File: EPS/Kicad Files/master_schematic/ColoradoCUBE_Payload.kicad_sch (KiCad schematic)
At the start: 8 parts, among them U1 PIC18F27Q84-E/SP

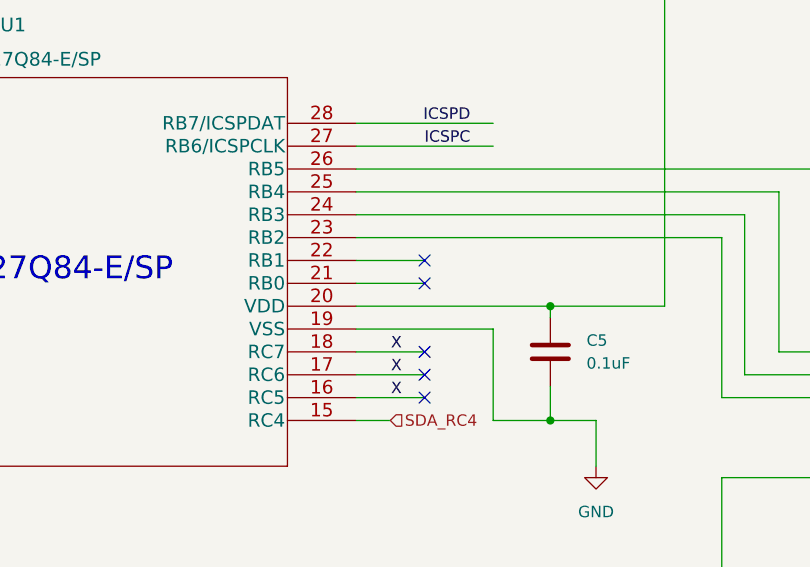
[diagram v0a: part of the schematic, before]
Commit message: revised EPS schematics
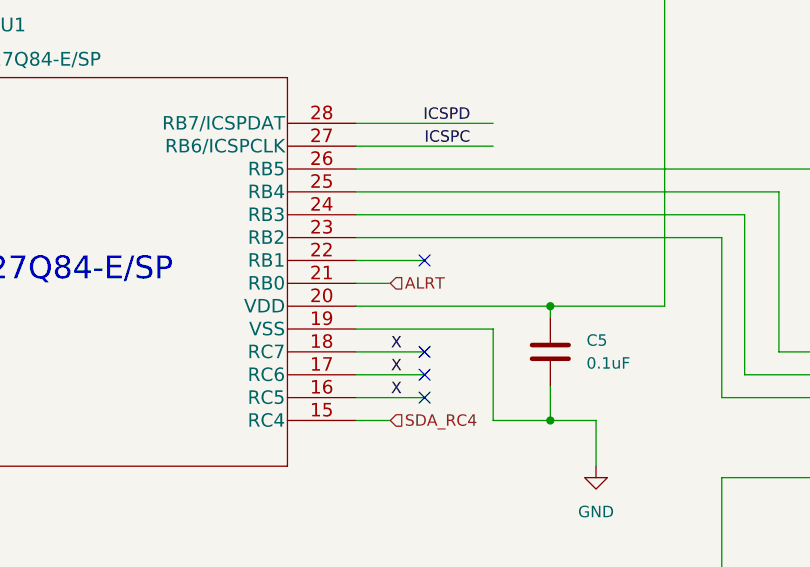
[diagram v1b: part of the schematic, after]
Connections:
- net ALRT: now reaches U1.21 (RB0)
- no-connect marks 11 -> 10
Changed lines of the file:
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@@
   (no_connect (at 238.76 132.08))
   (no_connect (at 238.76 134.62))
-  (no_connect (at 238.76 121.92))
   (no_connect (at 238.76 119.38))
   (no_connect (at 147.32 119.38))
@@
     (stroke (width 0) (type default) (color 0 0 0 0))
   )
+  (wire (pts (xy 231.14 121.92) (xy 234.95 121.92))
+    (stroke (width 0) (type default) (color 0 0 0 0))
+  )
   (wire (pts (xy 74.93 158.75) (xy 95.25 158.75))
     (stroke (width 0) (type default) (color 0 0 0 0))
   )
   (wire (pts (xy 271.78 116.84) (xy 231.14 116.84))
-    (stroke (width 0) (type default) (color 0 0 0 0))
-  )
-  (wire (pts (xy 231.14 121.92) (xy 238.76 121.92))
     (stroke (width 0) (type default) (color 0 0 0 0))
   )
@@
     (effects (font (size 1.27 1.27)) (justify left))
   )
+  (hierarchical_label "ALRT" (shape input) (at 234.95 121.92 0)
+    (effects (font (size 1.27 1.27)) (justify left))
+  )
   (hierarchical_label "CANL" (shape output) (at 347.98 138.43 0)
     (effects (font (size 1.27 1.27)) (justify left))
@@
   (symbol (lib_id "power:GND") (at 142.24 124.46 0) (unit 1)
     (in_bom yes) (on_board yes) (fields_autoplaced)
-    (property "Reference" "#PWR0102" (id 0) (at 142.24 130.81 0)
+    (property "Reference" "#PWR0122" (id 0) (at 142.24 130.81 0)
       (effects (font (size 1.27 1.27)) hide)
     )
@@
   (symbol (lib_id "power:GND") (at 128.27 142.24 0) (unit 1)
     (in_bom yes) (on_board yes) (fields_autoplaced)
-    (property "Reference" "#PWR01" (id 0) (at 128.27 148.59 0)
+    (property "Reference" "#PWR0123" (id 0) (at 128.27 148.59 0)
       (effects (font (size 1.27 1.27)) hide)
     )
@@
   (symbol (lib_id "power:GND") (at 271.78 161.29 0) (unit 1)
     (in_bom yes) (on_board yes) (fields_autoplaced)
-    (property "Reference" "#PWR0101" (id 0) (at 271.78 167.64 0)
-      (effects (font (size 1.27 1.27)) hide)
-    )
+    (property "Reference" "#PWR0124" (id 0) (at 271.78 167.64 0)
+      (effects (font (size 1.27 1.27)) hide)
+    )

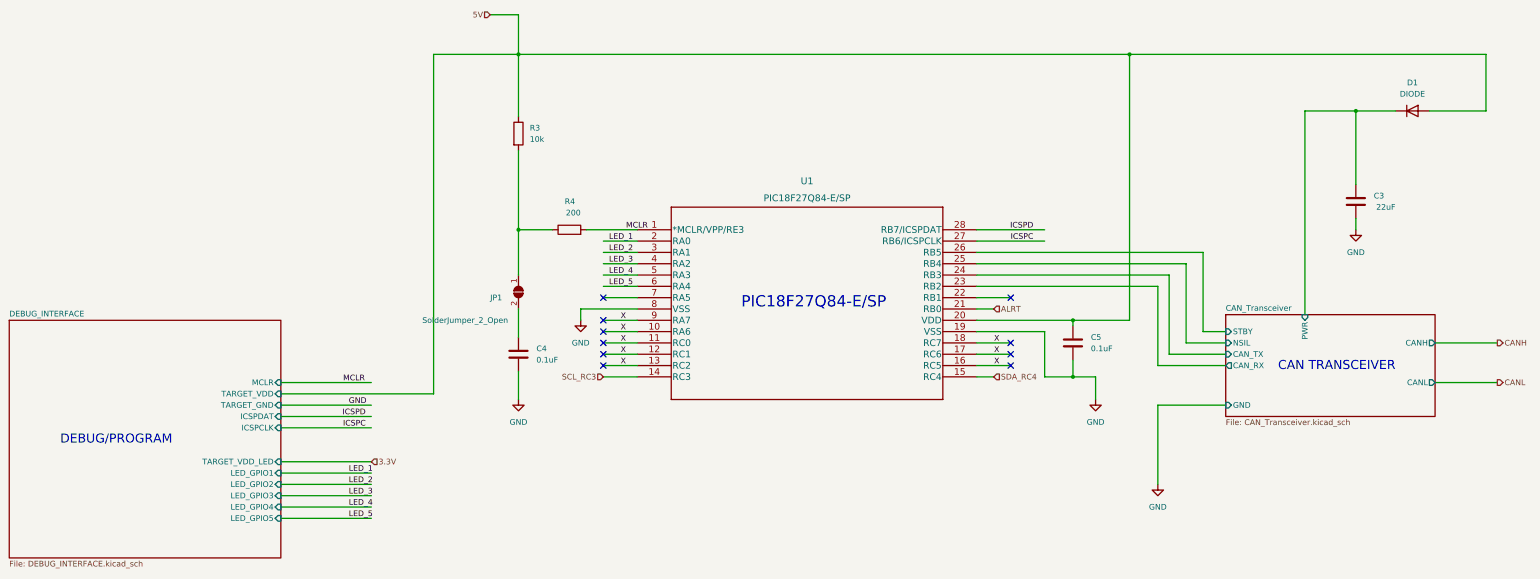
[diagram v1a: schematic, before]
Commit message: updated master schematic
should be nearing final schematic revision. run electrical rules check next
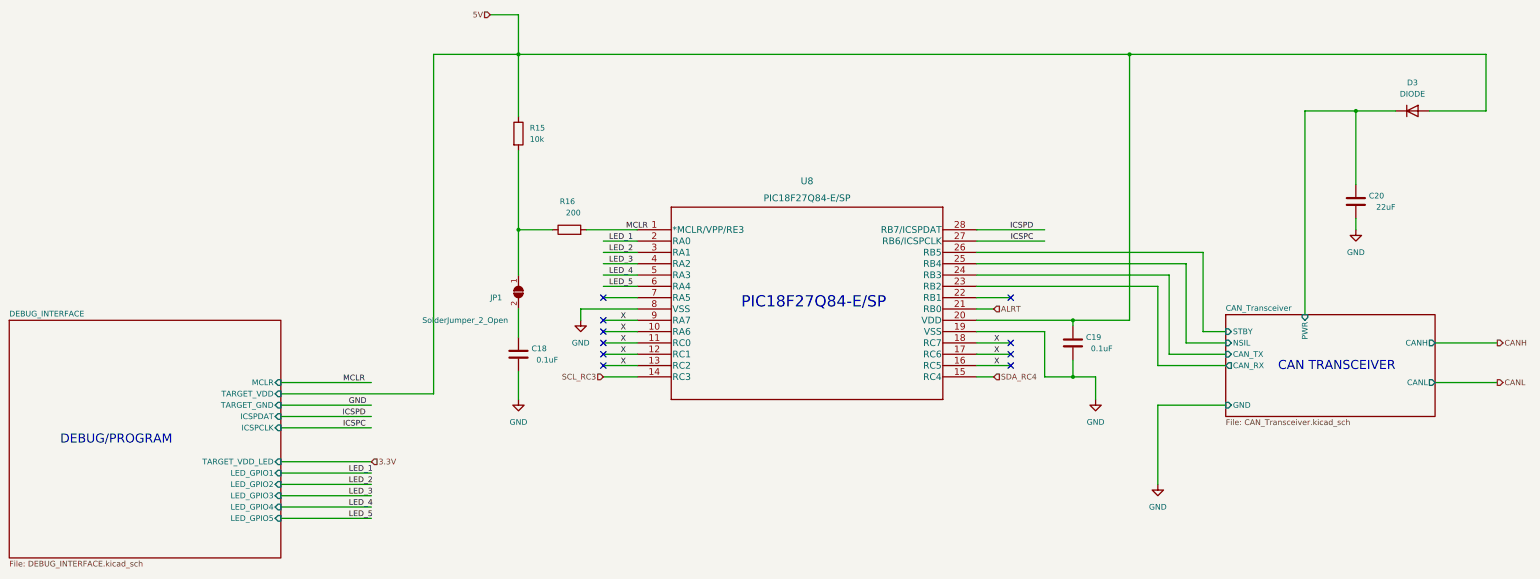
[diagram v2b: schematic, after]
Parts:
- C18: renamed from C4; footprint Capacitor_SMD:C_0603_1608Metric_Pad1.08x0.95mm_HandSolder -> Capacitor_SMD:C_0603_1608Metric
- C19: renamed from C5; footprint Capacitor_SMD:C_0603_1608Metric_Pad1.08x0.95mm_HandSolder -> Capacitor_SMD:C_0603_1608Metric
- C20: renamed from C3; footprint Capacitor_SMD:C_0603_1608Metric_Pad1.08x0.95mm_HandSolder -> Capacitor_SMD:C_0603_1608Metric
- D3: renamed from D1; footprint Diode_SMD:D_0805_2012Metric_Pad1.15x1.40mm_HandSolder -> Diode_SMD:D_0805_2012Metric
- R15: renamed from R3; footprint Resistor_SMD:R_0603_1608Metric_Pad0.98x0.95mm_HandSolder -> Resistor_SMD:R_0603_1608Metric
- R16: renamed from R4; footprint Resistor_SMD:R_0603_1608Metric_Pad0.98x0.95mm_HandSolder -> Resistor_SMD:R_0603_1608Metric
- renumbered U1 to U8
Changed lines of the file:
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@@
   (symbol (lib_id "power:GND") (at 142.24 124.46 0) (unit 1)
     (in_bom yes) (on_board yes) (fields_autoplaced)
-    (property "Reference" "#PWR0122" (id 0) (at 142.24 130.81 0)
+    (property "Reference" "#PWR024" (id 0) (at 142.24 130.81 0)
       (effects (font (size 1.27 1.27)) hide)
     )
@@
   (symbol (lib_id "2022-01-25_01-41-04:PIC18F27Q84-E{slash}SP") (at 154.94 104.14 0) (unit 1)
     (in_bom yes) (on_board yes) (fields_autoplaced)
-    (property "Reference" "U1" (id 0) (at 193.04 93.218 0)
+    (property "Reference" "U8" (id 0) (at 193.04 93.218 0)
       (effects (font (size 1.524 1.524)))
     )
@@
   (symbol (lib_id "power:GND") (at 316.23 104.14 0) (unit 1)
     (in_bom yes) (on_board yes) (fields_autoplaced)
-    (property "Reference" "#PWR02" (id 0) (at 316.23 110.49 0)
+    (property "Reference" "#PWR027" (id 0) (at 316.23 110.49 0)
       (effects (font (size 1.27 1.27)) hide)
     )
@@
   (symbol (lib_id "Device:R") (at 139.7 104.14 90) (unit 1)
     (in_bom yes) (on_board yes)
-    (property "Reference" "R4" (id 0) (at 140.97 97.79 90)
+    (property "Reference" "R16" (id 0) (at 140.97 97.79 90)
       (effects (font (size 1.27 1.27)) (justify left))
     )
@@
       (effects (font (size 1.27 1.27)) (justify left))
     )
-    (property "Footprint" "Resistor_SMD:R_0603_1608Metric_Pad0.98x0.95mm_HandSolder" (id 2) (at 139.7 105.918 90)
+    (property "Footprint" "Resistor_SMD:R_0603_1608Metric" (id 2) (at 139.7 105.918 90)
       (effects (font (size 1.27 1.27)) hide)
     )
@@
   (symbol (lib_id "Simulation_SPICE:DIODE") (at 328.93 77.47 180) (unit 1)
     (in_bom yes) (on_board yes) (fields_autoplaced)
-    (property "Reference" "D1" (id 0) (at 328.93 71.12 0))
+    (property "Reference" "D3" (id 0) (at 328.93 71.12 0))
     (property "Value" "DIODE" (id 1) (at 328.93 73.66 0))
-    (property "Footprint" "Diode_SMD:D_0805_2012Metric_Pad1.15x1.40mm_HandSolder" (id 2) (at 328.93 77.47 0)
+    (property "Footprint" "Diode_SMD:D_0805_2012Metric" (id 2) (at 328.93 77.47 0)
       (effects (font (size 1.27 1.27)) hide)
     )
@@
   (symbol (lib_id "power:GND") (at 128.27 142.24 0) (unit 1)
     (in_bom yes) (on_board yes) (fields_autoplaced)
-    (property "Reference" "#PWR0123" (id 0) (at 128.27 148.59 0)
+    (property "Reference" "#PWR023" (id 0) (at 128.27 148.59 0)
       (effects (font (size 1.27 1.27)) hide)
     )
@@
   (symbol (lib_id "Device:C") (at 316.23 97.79 180) (unit 1)
     (in_bom yes) (on_board yes)
-    (property "Reference" "C3" (id 0) (at 322.58 96.52 0)
+    (property "Reference" "C20" (id 0) (at 322.58 96.52 0)
       (effects (font (size 1.27 1.27)) (justify left))
     )
@@
       (effects (font (size 1.27 1.27)) (justify left))
     )
-    (property "Footprint" "Capacitor_SMD:C_0603_1608Metric_Pad1.08x0.95mm_HandSolder" (id 2) (at 315.2648 93.98 0)
+    (property "Footprint" "Capacitor_SMD:C_0603_1608Metric" (id 2) (at 315.2648 93.98 0)
       (effects (font (size 1.27 1.27)) hide)
     )
@@
   (symbol (lib_id "power:GND") (at 257.81 142.24 0) (unit 1)
     (in_bom yes) (on_board yes) (fields_autoplaced)
-    (property "Reference" "#PWR03" (id 0) (at 257.81 148.59 0)
+    (property "Reference" "#PWR025" (id 0) (at 257.81 148.59 0)
       (effects (font (size 1.27 1.27)) hide)
     )
@@
   (symbol (lib_id "Device:C") (at 128.27 132.08 180) (unit 1)
     (in_bom yes) (on_board yes)
-    (property "Reference" "C4" (id 0) (at 134.62 130.81 0)
+    (property "Reference" "C18" (id 0) (at 134.62 130.81 0)
       (effects (font (size 1.27 1.27)) (justify left))
     )
@@
       (effects (font (size 1.27 1.27)) (justify left))
     )
-    (property "Footprint" "Capacitor_SMD:C_0603_1608Metric_Pad1.08x0.95mm_HandSolder" (id 2) (at 127.3048 128.27 0)
+    (property "Footprint" "Capacitor_SMD:C_0603_1608Metric" (id 2) (at 127.3048 128.27 0)
       (effects (font (size 1.27 1.27)) hide)
     )
@@
   (symbol (lib_id "power:GND") (at 271.78 161.29 0) (unit 1)
     (in_bom yes) (on_board yes) (fields_autoplaced)
-    (property "Reference" "#PWR0124" (id 0) (at 271.78 167.64 0)
+    (property "Reference" "#PWR026" (id 0) (at 271.78 167.64 0)
       (effects (font (size 1.27 1.27)) hide)
     )
@@
   (symbol (lib_id "Device:R") (at 128.27 82.55 0) (unit 1)
     (in_bom yes) (on_board yes)
-    (property "Reference" "R3" (id 0) (at 130.81 81.2799 0)
+    (property "Reference" "R15" (id 0) (at 130.81 81.2799 0)
       (effects (font (size 1.27 1.27)) (justify left))
     )
@@
       (effects (font (size 1.27 1.27)) (justify left))
     )
-    (property "Footprint" "Resistor_SMD:R_0603_1608Metric_Pad0.98x0.95mm_HandSolder" (id 2) (at 126.492 82.55 90)
+    (property "Footprint" "Resistor_SMD:R_0603_1608Metric" (id 2) (at 126.492 82.55 90)
       (effects (font (size 1.27 1.27)) hide)
     )
@@
   (symbol (lib_id "Device:C") (at 252.73 129.54 180) (unit 1)
     (in_bom yes) (on_board yes)
-    (property "Reference" "C5" (id 0) (at 259.08 128.27 0)
+    (property "Reference" "C19" (id 0) (at 259.08 128.27 0)
       (effects (font (size 1.27 1.27)) (justify left))
     )
@@
       (effects (font (size 1.27 1.27)) (justify left))
     )
-    (property "Footprint" "Capacitor_SMD:C_0603_1608Metric_Pad1.08x0.95mm_HandSolder" (id 2) (at 251.7648 125.73 0)
-      (effects (font (size 1.27 1.27)) hide)
-    )
+    (property "Footprint" "Capacitor_SMD:C_0603_1608Metric" (id 2) (at 251.7648 125.73 0)
+      (effects (font (size 1.27 1.27)) hide)
+    )

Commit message: EPS master netlist complete
dropped all parts onto pcb
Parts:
- U8: footprint footprints:PIC18F27Q84-E&slash_SP -> pic18f27:PIC18F27Q84-E&slash_SP
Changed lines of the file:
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@@
       (effects (font (size 1.524 1.524)))
     )
-    (property "Footprint" "footprints:PIC18F27Q84-E&slash_SP" (id 2) (at 193.04 98.044 0)
+    (property "Footprint" "pic18f27:PIC18F27Q84-E&slash_SP" (id 2) (at 193.04 98.044 0)
       (effects (font (size 1.524 1.524)) hide)
     )

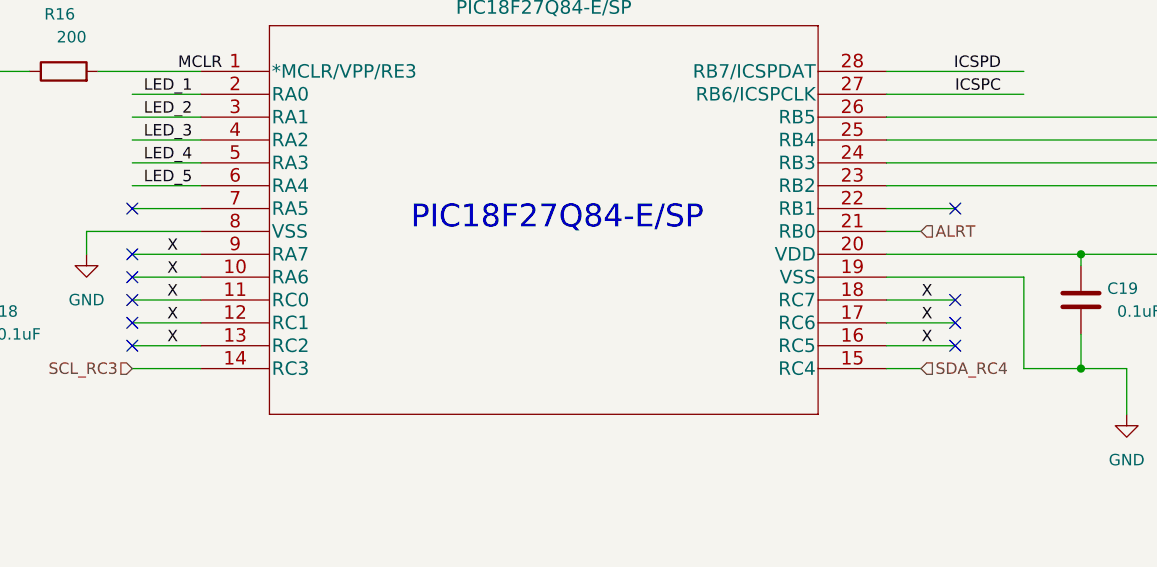
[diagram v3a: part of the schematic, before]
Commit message: all traces routed (EPS)
all nets, traces, etc connected.....now we need to run DRC...errors are inevitable
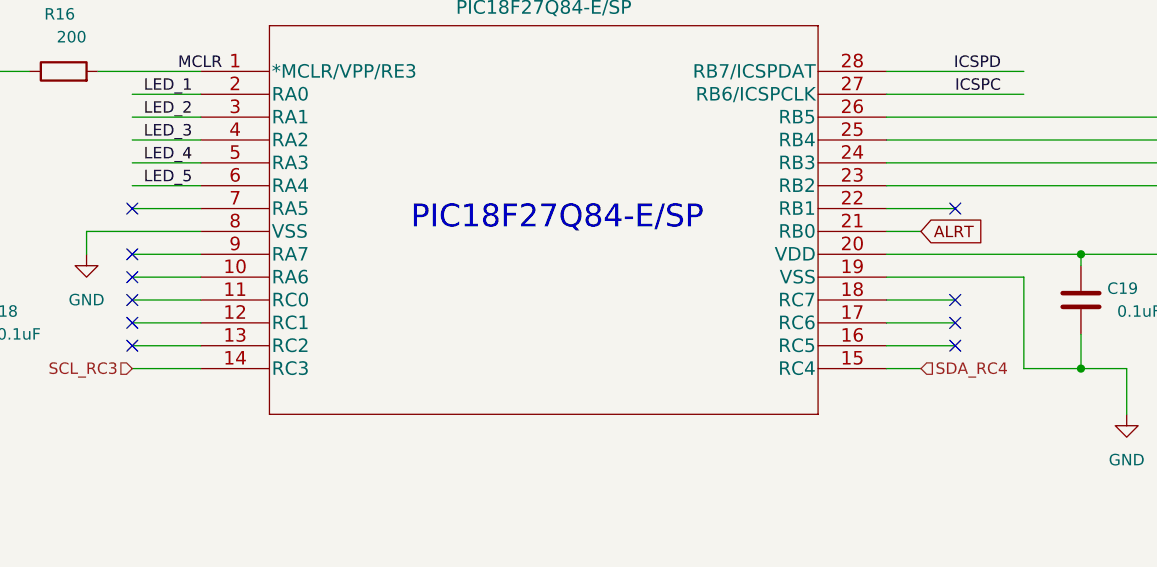
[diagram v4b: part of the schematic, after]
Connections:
- removed net X: U8.10 (RA6), U8.11 (RC0), U8.12 (RC1), U8.13 (RC2), U8.16 (RC5), U8.17 (RC6), U8.18 (RC7), U8.9 (RA7)
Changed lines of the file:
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@@
     (effects (font (size 2.032 2.032)) (justify right bottom))
-  )
-  (label "X" (at 236.22 134.62 180)
-    (effects (font (size 1.27 1.27)) (justify right bottom))
   )
   (label "LED_1" (at 148.59 106.68 0)
     (effects (font (size 1.27 1.27)) (justify left bottom))
-  )
-  (label "X" (at 236.22 129.54 180)
-    (effects (font (size 1.27 1.27)) (justify right bottom))
   )
   (label "LED_3" (at 148.59 111.76 0)
@@
   (label "MCLR" (at 152.4 104.14 0)
     (effects (font (size 1.27 1.27)) (justify left bottom))
-  )
-  (label "X" (at 152.4 127 180)
-    (effects (font (size 1.27 1.27)) (justify right bottom))
   )
   (label "ICSPD" (at 93.98 146.05 180)
@@
     (effects (font (size 1.27 1.27)) (justify left bottom))
   )
-  (label "X" (at 152.4 129.54 180)
-    (effects (font (size 1.27 1.27)) (justify right bottom))
-  )
-  (label "X" (at 152.4 134.62 180)
-    (effects (font (size 1.27 1.27)) (justify right bottom))
-  )
   (label "MCLR" (at 88.9 138.43 0)
     (effects (font (size 1.27 1.27)) (justify left bottom))
   )
-  (label "X" (at 152.4 124.46 180)
-    (effects (font (size 1.27 1.27)) (justify right bottom))
-  )
   (label "LED_1" (at 90.17 158.75 0)
     (effects (font (size 1.27 1.27)) (justify left bottom))
-  )
-  (label "X" (at 152.4 132.08 180)
-    (effects (font (size 1.27 1.27)) (justify right bottom))
   )
   (label "ICSPC" (at 243.84 106.68 180)
@@
     (effects (font (size 1.27 1.27)) (justify left bottom))
   )
-  (label "X" (at 236.22 132.08 180)
-    (effects (font (size 1.27 1.27)) (justify right bottom))
-  )
   (label "LED_2" (at 90.17 161.29 0)
     (effects (font (size 1.27 1.27)) (justify left bottom))
@@
   (label "ICSPD" (at 243.84 104.14 180)
     (effects (font (size 1.27 1.27)) (justify right bottom))
+  )
+  (global_label "ALRT" (shape input) (at 234.95 121.92 0) (fields_autoplaced)
+    (effects (font (size 1.27 1.27)) (justify left))
+    (property "Intersheet References" "${INTERSHEET_REFS}" (id 0) (at 241.7174 121.8406 0)
+      (effects (font (size 1.27 1.27)) (justify left) hide)
+    )
   )
   (hierarchical_label "CANH" (shape output) (at 347.98 129.54 0)
@@
     (effects (font (size 1.27 1.27)) (justify left))
   )
-  (hierarchical_label "ALRT" (shape input) (at 234.95 121.92 0)
-    (effects (font (size 1.27 1.27)) (justify left))
-  )

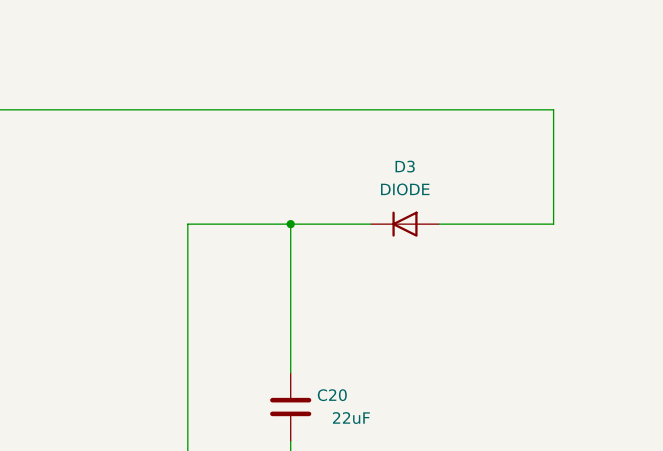
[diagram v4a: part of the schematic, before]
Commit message: Eps board update
vias fixed for manufacturers standards, eliminated ALRT pin on battery gauge
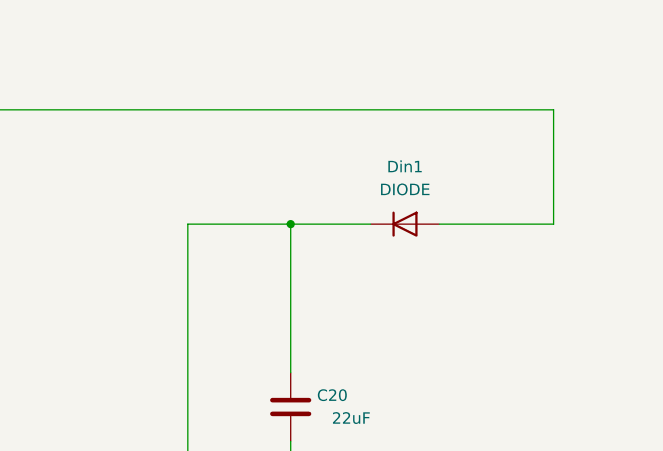
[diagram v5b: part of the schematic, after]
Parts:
- renumbered D3 to Din1
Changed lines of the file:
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@@
   (symbol (lib_id "Simulation_SPICE:DIODE") (at 328.93 77.47 180) (unit 1)
     (in_bom yes) (on_board yes) (fields_autoplaced)
-    (property "Reference" "D3" (id 0) (at 328.93 71.12 0))
+    (property "Reference" "Din1" (id 0) (at 328.93 71.12 0))
     (property "Value" "DIODE" (id 1) (at 328.93 73.66 0))
     (property "Footprint" "Diode_SMD:D_0805_2012Metric" (id 2) (at 328.93 77.47 0)
